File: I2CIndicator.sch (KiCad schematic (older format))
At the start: 19 parts, among them Q1 BS107, Q2 BS107, Q3 BS107, U1 PCA9685

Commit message: Modified to use SunLED XZCB25MO24DG25X111S
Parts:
- removed D6: LED_RGB, LEDs:LED_RGB_PLLC-6_HandSoldering, symbol LED_RGB
- added D6: LED_BRG_EP, LEDs:SunLED-XZ, symbol LED_BRG_EP
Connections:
- wire segments 77 -> 63
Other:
- moved on the sheet: C1, D1, D2, D3, D4, D5, Q1, Q2, Q3, R1, R2, R3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

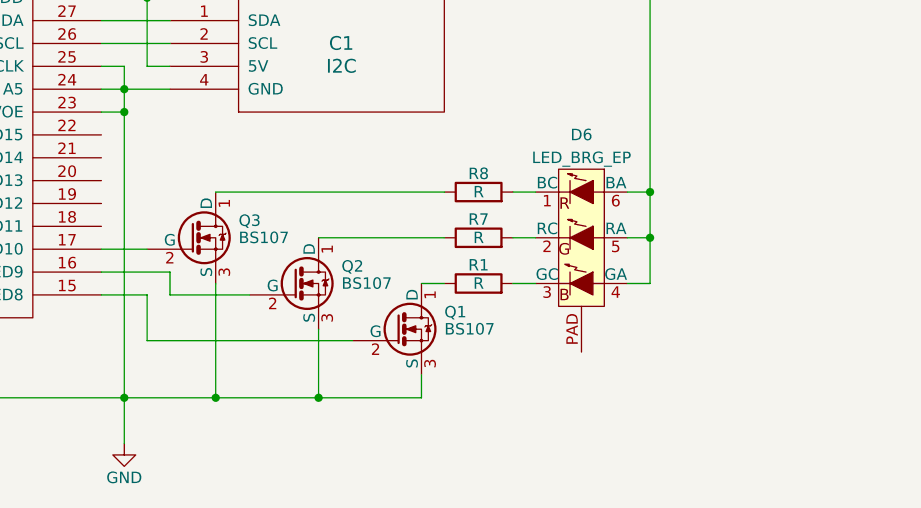
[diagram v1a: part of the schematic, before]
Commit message: Found wrong component was used for N-MOSFET transistors resulting in wrong layout. Fixed schamatic, but layout needs to be fixed.
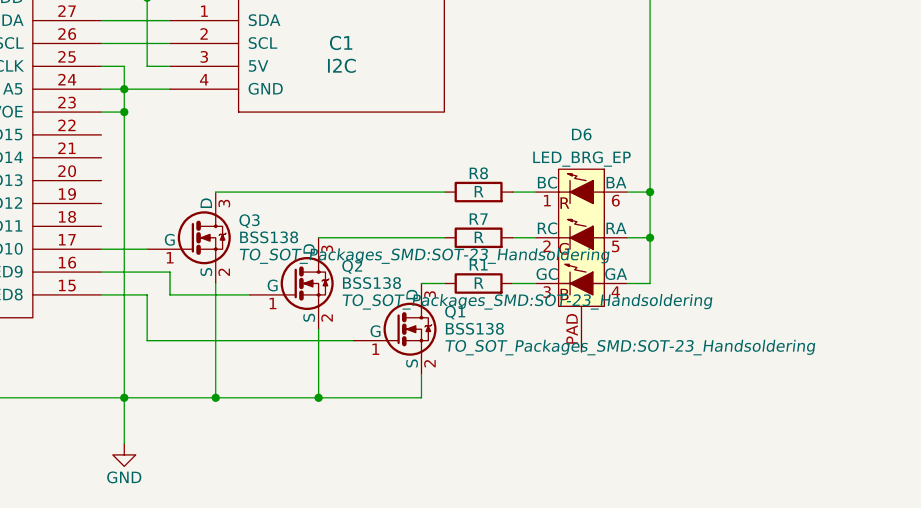
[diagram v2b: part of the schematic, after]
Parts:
- removed Q1, Q2, Q3: BS107, TO_SOT_Packages_SMD:SOT-23_Handsoldering, symbol BS107
- added Q1, Q2, Q3: BSS138, TO_SOT_Packages_SMD:SOT-23_Handsoldering, symbol BSS138
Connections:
- net GND: now also Q1.2 (S), Q2.2 (S), Q3.2 (S)
- net at U1.15 (LED8): now also Q1.1 (G)
- net at U1.16 (LED9): now also Q2.1 (G)
- net at U1.17 (LED10): now also Q3.1 (G)
- net at R8.1: now also Q3.3 (D)
- net at R7.1: now also Q2.3 (D)
- net at R1.1: now also Q1.3 (D)
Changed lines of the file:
@@
 LIBS:miscellaneous
 LIBS:I2CIndicator
+LIBS:I2CIndicator-cache
 EELAYER 25 0
 EELAYER END
@@
 $EndComp
 $Comp
-L BS107 Q3
-U 1 1 56EEC885
-P 5950 3650
-F 0 "Q3" H 6150 3725 50  0000 L CNN
-F 1 "BS107" H 6150 3650 50  0000 L CNN
-F 2 "TO_SOT_Packages_SMD:SOT-23_Handsoldering" H 6150 3575 50  0001 L CIN
-F 3 "" H 5950 3650 50  0000 L CNN
-	1    5950 3650
-	1    0    0    -1
-$EndComp
-$Comp
-L BS107 Q2
-U 1 1 56F00F08
-P 6400 3850
-F 0 "Q2" H 6600 3925 50  0000 L CNN
-F 1 "BS107" H 6600 3850 50  0000 L CNN
-F 2 "TO_SOT_Packages_SMD:SOT-23_Handsoldering" H 6600 3775 50  0001 L CIN
-F 3 "" H 6400 3850 50  0000 L CNN
-	1    6400 3850
-	1    0    0    -1
-$EndComp
-$Comp
 L +5V #PWR01
 U 1 1 56F01257
@@
 $EndComp
 $Comp
-L BS107 Q1
-U 1 1 56F00F39
-P 6850 4050
-F 0 "Q1" H 7050 4125 50  0000 L CNN
-F 1 "BS107" H 7050 4050 50  0000 L CNN
-F 2 "TO_SOT_Packages_SMD:SOT-23_Handsoldering" H 7050 3975 50  0001 L CIN
-F 3 "" H 6850 4050 50  0000 L CNN
-	1    6850 4050
-	1    0    0    -1
-$EndComp
-$Comp
 L R R1
 U 1 1 56F02F65
@@
 	7950 3850 7850 3850
 Connection ~ 7950 3650
+$Comp
+L BSS138 Q1
+U 1 1 5843BFF4
+P 6850 4050
+F 0 "Q1" H 7050 4125 50  0000 L CNN
+F 1 "BSS138" H 7050 4050 50  0000 L CNN
+F 2 "TO_SOT_Packages_SMD:SOT-23_Handsoldering" H 7050 3975 50  0000 L CIN
+F 3 "" H 6850 4050 50  0000 L CNN
+	1    6850 4050
+	1    0    0    -1
+$EndComp
+$Comp
+L BSS138 Q2
+U 1 1 5843C1E6
+P 6400 3850
+F 0 "Q2" H 6600 3925 50  0000 L CNN
+F 1 "BSS138" H 6600 3850 50  0000 L CNN
+F 2 "TO_SOT_Packages_SMD:SOT-23_Handsoldering" H 6600 3775 50  0000 L CIN
+F 3 "" H 6400 3850 50  0000 L CNN
+	1    6400 3850
+	1    0    0    -1
+$EndComp
+$Comp
+L BSS138 Q3
+U 1 1 5843C249
+P 5950 3650
+F 0 "Q3" H 6150 3725 50  0000 L CNN
+F 1 "BSS138" H 6150 3650 50  0000 L CNN
+F 2 "TO_SOT_Packages_SMD:SOT-23_Handsoldering" H 6150 3575 50  0000 L CIN
+F 3 "" H 5950 3650 50  0000 L CNN
+	1    5950 3650
+	1    0    0    -1
+$EndComp
 $EndSCHEMATC
